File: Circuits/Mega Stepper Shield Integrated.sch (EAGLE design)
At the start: 69 parts, among them IC1 MC33269ST-5.0T3, IC2 MC33269D-5.0, IC3 ATMEGA2560-16AU, IC4 ATMEGA8U2-MU, IC5 LM358D, IC6 LP2985-33DBVR, Q2 16MHz, T1 2N2222, T2 FDN340P, Y1 16MHz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

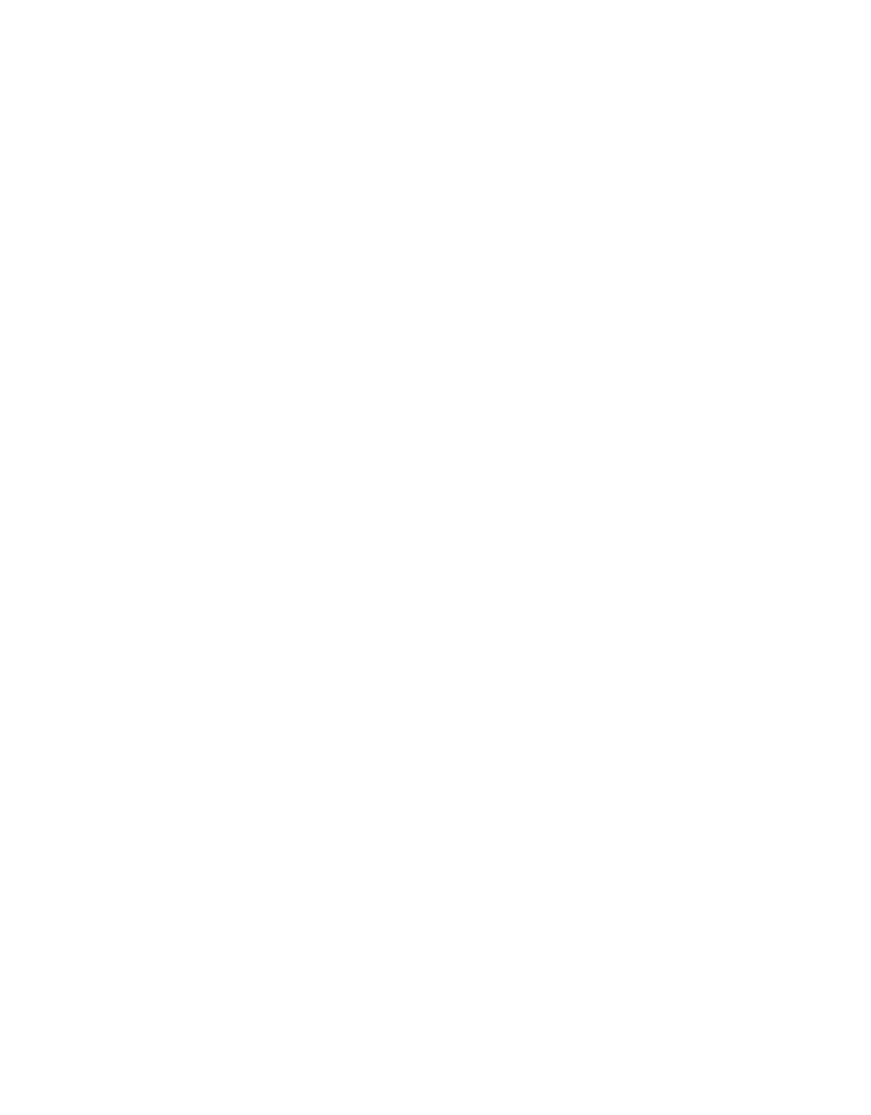
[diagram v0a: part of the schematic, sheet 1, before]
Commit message: Create Integrated Version of Board
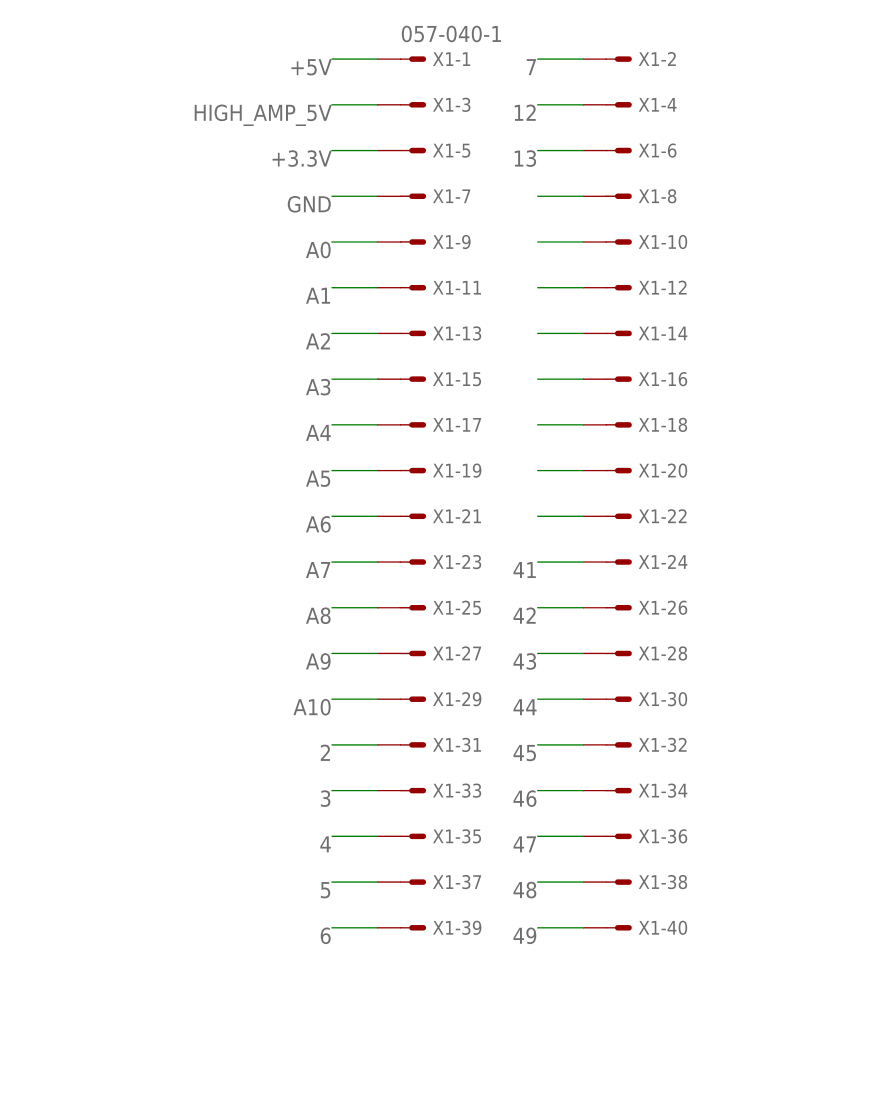
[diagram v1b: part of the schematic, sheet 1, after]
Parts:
- added X1: 057-040-1, con-panduit:057-040-1
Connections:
- new net 16: X1-8.S
- new net N$44: X1-10.S
- new net N$45: X1-12.S
- new net N$46: X1-14.S
- new net N$47: X1-16.S
- new net N$48: X1-18.S
- new net N$49: X1-20.S
- net +3.3V: now also X1-5.S
- net +5V: now also X1-1.S
- net 12: now also X1-4.S
- net 13: now also X1-6.S
- net 2: now also X1-31.S
- net 3: now also X1-33.S
- net 4: now also X1-35.S
- net 40: now also X1-22.S
- net 41: now also X1-24.S
- net 42: now also X1-26.S
- net 43: now also X1-28.S
- net 44: now also X1-30.S
- net 45: now also X1-32.S
- net 46: now also X1-34.S
- net 47: now also X1-36.S
- net 48: now also X1-38.S
- net 49: now also X1-40.S
- net 5: now also X1-37.S
- net 6: now also X1-39.S
- net 7: now also X1-2.S
- net A0: now also X1-9.S
- net A1: now also X1-11.S
- net A10: now also X1-29.S
- net A2: now also X1-13.S
- net A3: now also X1-15.S
- net A4: now also X1-17.S
- net A5: now also X1-19.S
- net A6: now also X1-21.S
- net A7: now also X1-23.S
- net A8: now also X1-25.S
- net A9: now also X1-27.S
- net GND: now also X1-7.S
- net HIGH_AMP_5V: now also X1-3.S
